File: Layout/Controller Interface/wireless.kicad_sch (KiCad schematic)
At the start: 1 part

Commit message: Completed schematic and layout
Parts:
- removed U6: ~, RF_Module:nRF24L01_Mini, symbol RF:NRF24L01_Mini
- added D1 (x2): LED, LED_SMD:LED_0805_2012Metric, symbol Device:LED
- added R4 (x2): 100, Resistor_SMD:R_0805_2012Metric, symbol Device:R_US
- added U3: ~, GTS24:GTS24-SMD, symbol GTS24:GTS24
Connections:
- net +3.3V: now also U3.1 (VCC)
- net GND: now also D1.1 (K), D1.1 (K), U3.8 (GND)
- net NRF_CE: now also U3.2 (~{CE})
- net NRF_CS: now also U3.3 (~{CS})
- net NRF_IRQ: now also U3.7 (IRQ)
- net SPI0_CLK: now also U3.4 (SCK)
- net SPI0_MISO: now also U3.6 (MISO)
- net SPI0_MOSI: now also U3.5 (MOSI)
- new net: D1.2 (A), R4.2 (x2)
- new net RX_LED: R4.1
- new net TX_LED: R4.1

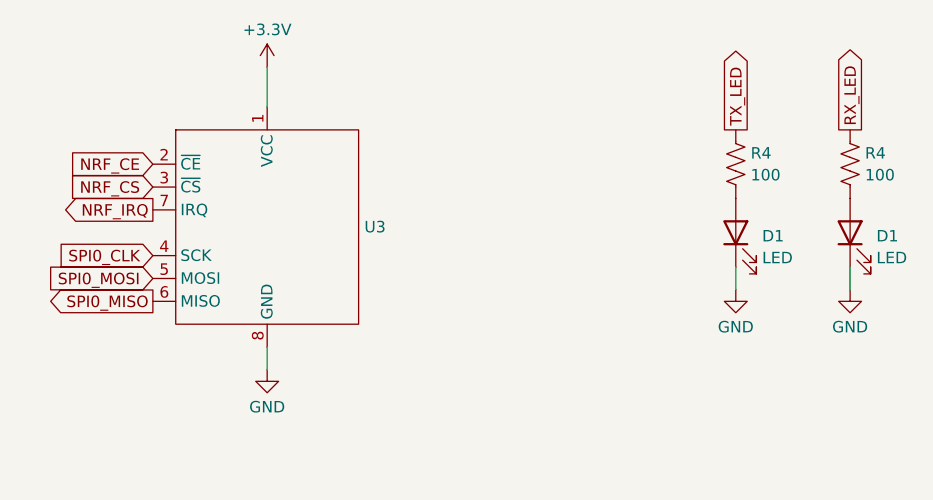
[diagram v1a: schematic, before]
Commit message: Create a separate board for the LEDs
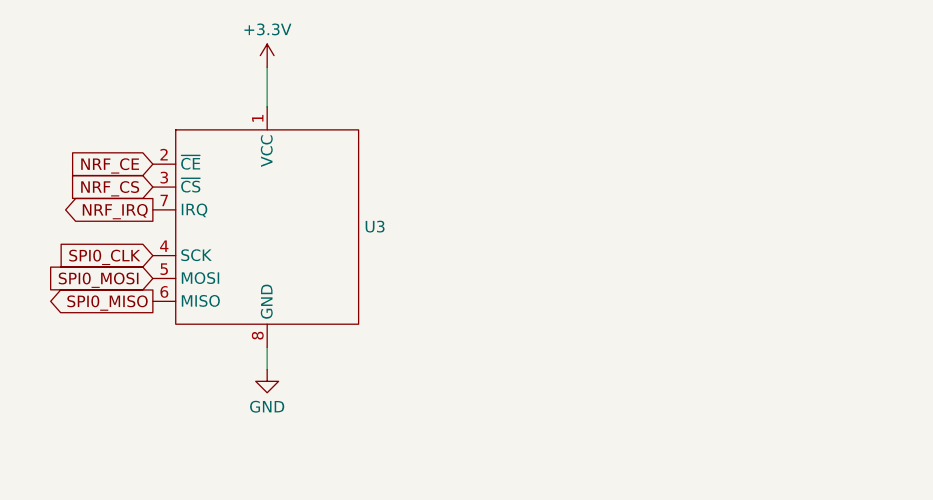
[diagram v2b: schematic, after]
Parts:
- removed D1 (x2): LED, LED_SMD:LED_0805_2012Metric, symbol Device:LED
- removed R4 (x2): 100, Resistor_SMD:R_0805_2012Metric, symbol Device:R_US
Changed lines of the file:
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@@
-    (stroke (width 0) (type default))
-  )
-  (wire (pts (xy 199.39 86.36) (xy 199.39 88.9))
-    (stroke (width 0) (type default))
-  )
-  (wire (pts (xy 186.69 86.36) (xy 186.69 88.9))
     (stroke (width 0) (type default))
   )
@@
     (property "Intersheetrefs" "${INTERSHEET_REFS}" (at 110.1053 85.09 0)
       (effects (font (size 1.27 1.27)) (justify right) hide)
-    )
-  )
-  (global_label "TX_LED" (shape output) (at 186.69 71.12 90) (fields_autoplaced)
-    (effects (font (size 1.27 1.27)) (justify left))
-    (property "Intersheetrefs" "${INTERSHEET_REFS}" (at 186.69 61.543 90)
-      (effects (font (size 1.27 1.27)) (justify left) hide)
     )
   )
@@
     )
   )
-  (global_label "RX_LED" (shape output) (at 199.39 71.12 90) (fields_autoplaced)
-    (effects (font (size 1.27 1.27)) (justify left))
-    (property "Intersheetrefs" "${INTERSHEET_REFS}" (at 199.39 61.2406 90)
-      (effects (font (size 1.27 1.27)) (justify left) hide)
-    )
-  )
   (global_label "NRF_CE" (shape input) (at 121.92 74.93 180) (fields_autoplaced)
     (effects (font (size 1.27 1.27)) (justify right))
@@
     (property "Intersheetrefs" "${INTERSHEET_REFS}" (at 109.0772 90.17 0)
       (effects (font (size 1.27 1.27)) (justify right) hide)
-    )
-  )
-  (symbol (lib_id "power:GND") (at 199.39 88.9 0) (unit 1)
-    (in_bom yes) (on_board yes) (dnp no) (fields_autoplaced)
-    (property "Reference" "#PWR013" (at 199.39 95.25 0)
-      (effects (font (size 1.27 1.27)) hide)
-    )
-    (property "Value" "GND" (at 199.39 93.0331 0)
-      (effects (font (size 1.27 1.27)))
-    )
-    (property "Footprint" "" (at 199.39 88.9 0)
-      (effects (font (size 1.27 1.27)) hide)
-    )
-    (property "Datasheet" "" (at 199.39 88.9 0)
-      (effects (font (size 1.27 1.27)) hide)
-    )
-    (pin "1")
-    (instances
-      (project "Controller Interface"
-        (path "/debf4462-021e-4805-bcd2-6130c1f65c4c/8b74bfbb-1df7-41c8-9da7-14534e77ff25"
-          (reference "#PWR013") (unit 1)
-        )
-        (path "/debf4462-021e-4805-bcd2-6130c1f65c4c/00d40970-3d04-492a-a76f-db39fb68e165"
-          (reference "#PWR058") (unit 1)
-        )
-      )
     )
   )
@@
     )
   )
-  (symbol (lib_id "Device:R_US") (at 186.69 74.93 0) (unit 1)
-    (in_bom yes) (on_board yes) (dnp no) (fields_autoplaced)
-    (property "Reference" "R4" (at 188.341 73.7179 0)
-      (effects (font (size 1.27 1.27)) (justify left))
-    )
-    (property "Value" "100" (at 188.341 76.1421 0)
-      (effects (font (size 1.27 1.27)) (justify left))
-    )
-    (property "Footprint" "Resistor_SMD:R_0805_2012Metric" (at 187.706 75.184 90)
-      (effects (font (size 1.27 1.27)) hide)
-    )
-    (property "Datasheet" "~" (at 186.69 74.93 0)
-      (effects (font (size 1.27 1.27)) hide)
-    )
-    (pin "1")
-    (pin "2")
-    (instances
-      (project "Controller Interface"
-        (path "/debf4462-021e-4805-bcd2-6130c1f65c4c/8b74bfbb-1df7-41c8-9da7-14534e77ff25"
-          (reference "R4") (unit 1)
-        )
-        (path "/debf4462-021e-4805-bcd2-6130c1f65c4c/00d40970-3d04-492a-a76f-db39fb68e165"
-          (reference "R19") (unit 1)
-        )
-      )
-    )
-  )
-  (symbol (lib_id "Device:R_US") (at 199.39 74.93 0) (unit 1)
-    (in_bom yes) (on_board yes) (dnp no) (fields_autoplaced)
-    (property "Reference" "R4" (at 201.041 73.7179 0)
-      (effects (font (size 1.27 1.27)) (justify left))
-    )
-    (property "Value" "100" (at 201.041 76.1421 0)
-      (effects (font (size 1.27 1.27)) (justify left))
-    )
-    (property "Footprint" "Resistor_SMD:R_0805_2012Metric" (at 200.406 75.184 90)
-      (effects (font (size 1.27 1.27)) hide)
-    )
-    (property "Datasheet" "~" (at 199.39 74.93 0)
-      (effects (font (size 1.27 1.27)) hide)
-    )
-    (pin "1")
-    (pin "2")
-    (instances
-      (project "Controller Interface"
-        (path "/debf4462-021e-4805-bcd2-6130c1f65c4c/8b74bfbb-1df7-41c8-9da7-14534e77ff25"
-          (reference "R4") (unit 1)
-        )
-        (path "/debf4462-021e-4805-bcd2-6130c1f65c4c/00d40970-3d04-492a-a76f-db39fb68e165"
-          (reference "R20") (unit 1)
-        )
-      )
-    )
-  )
-  (symbol (lib_id "Device:LED") (at 199.39 82.55 90) (unit 1)
-    (in_bom yes) (on_board yes) (dnp no) (fields_autoplaced)
-    (property "Reference" "D1" (at 202.311 82.9254 90)
-      (effects (font (size 1.27 1.27)) (justify right))
-    )
-    (property "Value" "LED" (at 202.311 85.3496 90)
-      (effects (font (size 1.27 1.27)) (justify right))
-    )
-    (property "Footprint" "LED_SMD:LED_0805_2012Metric" (at 199.39 82.55 0)
-      (effects (font (size 1.27 1.27)) hide)
-    )
-    (property "Datasheet" "~" (at 199.39 82.55 0)
-      (effects (font (size 1.27 1.27)) hide)
-    )
-    (pin "1")
-    (pin "2")
-    (instances
-      (project "Controller Interface"
-        (path "/debf4462-021e-4805-bcd2-6130c1f65c4c/8b74bfbb-1df7-41c8-9da7-14534e77ff25"
-          (reference "D1") (unit 1)
-        )
-        (path "/debf4462-021e-4805-bcd2-6130c1f65c4c/00d40970-3d04-492a-a76f-db39fb68e165"
-          (reference "D9") (unit 1)
-        )
-      )
-    )
-  )
-  (symbol (lib_id "Device:LED") (at 186.69 82.55 90) (unit 1)
-    (in_bom yes) (on_board yes) (dnp no) (fields_autoplaced)
-    (property "Reference" "D1" (at 189.611 82.9254 90)
-      (effects (font (size 1.27 1.27)) (justify right))
-    )
-    (property "Value" "LED" (at 189.611 85.3496 90)
-      (effects (font (size 1.27 1.27)) (justify right))
-    )
-    (property "Footprint" "LED_SMD:LED_0805_2012Metric" (at 186.69 82.55 0)
-      (effects (font (size 1.27 1.27)) hide)
-    )
-    (property "Datasheet" "~" (at 186.69 82.55 0)
-      (effects (font (size 1.27 1.27)) hide)
-    )
-    (pin "1")
-    (pin "2")
-    (instances
-      (project "Controller Interface"
-        (path "/debf4462-021e-4805-bcd2-6130c1f65c4c/8b74bfbb-1df7-41c8-9da7-14534e77ff25"
-          (reference "D1") (unit 1)
-        )
-        (path "/debf4462-021e-4805-bcd2-6130c1f65c4c/00d40970-3d04-492a-a76f-db39fb68e165"
-          (reference "D8") (unit 1)
-        )
-      )
-    )
-  )
   (symbol (lib_id "power:GND") (at 134.62 97.79 0) (unit 1)
     (in_bom yes) (on_board yes) (dnp no) (fields_autoplaced)
@@
         )
       )
-    )
-  )
-  (symbol (lib_id "power:GND") (at 186.69 88.9 0) (unit 1)
-    (in_bom yes) (on_board yes) (dnp no) (fields_autoplaced)
-    (property "Reference" "#PWR013" (at 186.69 95.25 0)
-      (effects (font (size 1.27 1.27)) hide)
-    )
-    (property "Value" "GND" (at 186.69 93.0331 0)
-      (effects (font (size 1.27 1.27)))
-    )
-    (property "Footprint" "" (at 186.69 88.9 0)
-      (effects (font (size 1.27 1.27)) hide)
-    )
-    (property "Datasheet" "" (at 186.69 88.9 0)
-      (effects (font (size 1.27 1.27)) hide)
-    )
-    (pin "1")
-    (instances
-      (project "Controller Interface"
-        (path "/debf4462-021e-4805-bcd2-6130c1f65c4c/8b74bfbb-1df7-41c8-9da7-14534e77ff25"
-          (reference "#PWR013") (unit 1)
-        )
-        (path "/debf4462-021e-4805-bcd2-6130c1f65c4c/00d40970-3d04-492a-a76f-db39fb68e165"
-          (reference "#PWR057") (unit 1)
-        )
-      )
